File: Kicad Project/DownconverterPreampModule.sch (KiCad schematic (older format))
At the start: 15 parts, among them U1 GALI-1+, U2 MCA1-85L+, U4 LMV751

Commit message: PCB Changes
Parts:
- added J6: Conn_01x02, Pin_Headers:Pin_Header_Straight_1x02_Pitch1.27mm, symbol Conn_01x02
- C2: footprint RadarComponents:100PAD -> RadarComponents:100PAD+GND2
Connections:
- net GND: now also J6.1 (Pin_1)
- net at R6.2, U4.1 (VOUT): now also J6.2 (Pin_2)
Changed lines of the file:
@@
 F 0 "C2" H 3225 3400 50  0000 L CNN
 F 1 "270pF" H 3225 3200 50  0000 L CNN
-F 2 "RadarComponents:100PAD" H 3238 3150 50  0001 C CNN
+F 2 "RadarComponents:100PAD+GND2" H 3238 3150 50  0001 C CNN
 F 3 "" H 3200 3300 50  0001 C CNN
 	1    3200 3300
@@
 $EndComp
 Wire Wire Line
-	7800 2200 7500 2200
-Wire Wire Line
-	7500 2200 7500 1000
-Wire Wire Line
-	7500 1000 8500 1000
-Text Notes 8600 1000 0    60   ~ 0
+	7500 2200 7800 2200
+Wire Wire Line
+	7500 900  7500 2200
+Text Notes 8900 850  0    60   ~ 0
 OUT
 $Comp
@@
 Wire Wire Line
 	7400 2800 7800 2800
+$Comp
+L Conn_01x02 J6
+U 1 1 5A0523B7
+P 8700 1000
+F 0 "J6" H 8700 1100 50  0000 C CNN
+F 1 "Conn_01x02" H 8700 800 50  0000 C CNN
+F 2 "Pin_Headers:Pin_Header_Straight_1x02_Pitch1.27mm" H 8700 1000 50  0001 C CNN
+F 3 "" H 8700 1000 50  0001 C CNN
+	1    8700 1000
+	1    0    0    1
+$EndComp
+$Comp
+L GND #PWR010
+U 1 1 5A05247F
+P 8500 1100
+F 0 "#PWR010" H 8500 850 50  0001 C CNN
+F 1 "GND" H 8500 950 50  0000 C CNN
+F 2 "" H 8500 1100 50  0001 C CNN
+F 3 "" H 8500 1100 50  0001 C CNN
+	1    8500 1100
+	1    0    0    -1
+$EndComp
+Wire Wire Line
+	7500 900  8500 900
+Wire Wire Line
+	8500 1000 8500 1100
 $EndSCHEMATC

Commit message: More PCB Updates
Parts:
- R2: footprint RadarComponents:100PAD -> RadarComponents:100PAD+GND
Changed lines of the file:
@@
 F 0 "R2" V 3330 2800 50  0000 C CNN
 F 1 "75" V 3250 2800 50  0000 C CNN
-F 2 "RadarComponents:100PAD" V 3180 2800 50  0001 C CNN
+F 2 "RadarComponents:100PAD+GND" V 3180 2800 50  0001 C CNN
 F 3 "" H 3250 2800 50  0001 C CNN
 	1    3250 2800

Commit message: PCB Edits post PDR
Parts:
- added R21: 51, Resistors_SMD:R_0603, symbol R
- C15, C4: value 270pF -> ?F
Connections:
- net +9V: no longer C16.1, U4.5 (V+)
- net GND: now also R21.1
- net at C15.2, U2.3 (IF): now also R21.2
- new net +3V3: C16.1, U4.5 (V+)
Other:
- moved on the sheet: C1, C15, C16, C2, C3, C4, J6, R1, R2, R3, R4, R5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

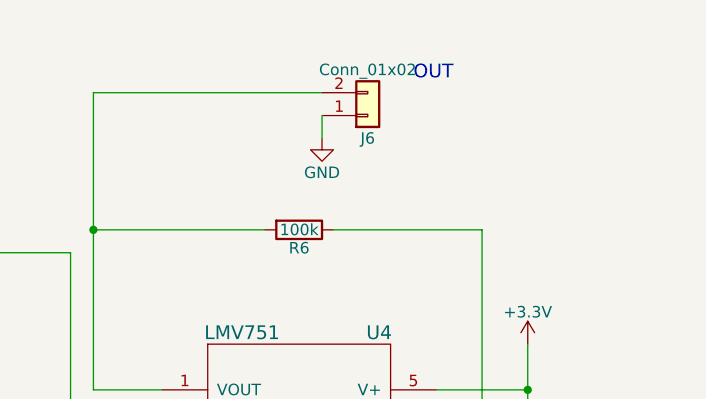
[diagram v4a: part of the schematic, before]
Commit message: Rev 2 update 1
Changes for Rev2:
Mounting Holes (duh)
Right Headers
HeadphoneJack
Added tantulum Caps at Regulators
Added UFL conns
Removed Resistive Divider
&
General layout stuff
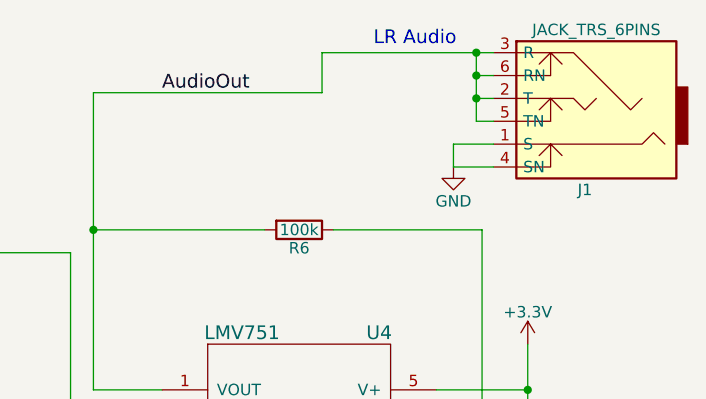
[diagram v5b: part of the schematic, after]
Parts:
- removed J6: Conn_01x02, Pin_Headers:Pin_Header_Straight_1x02_Pitch1.27mm, symbol Conn_01x02
- added J1: JACK_TRS_6PINS, RadarComponents:3.5mm_SMD, symbol JACK_TRS_6PINS
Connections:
- net GND: now also J1.1 (S), J1.4 (SN)
- net AudioOut: now reaches R6.2, U4.1 (VOUT)
- net AudioOut: now also J1.2 (T), J1.3 (R), J1.5 (TN), J1.6 (RN)
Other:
- note added: "LR Audio"
- note removed: "OUT"
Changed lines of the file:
@@
 Wire Wire Line
 	7950 975  7950 2275
-Text Notes 9350 925  0    60   ~ 0
-OUT
+Text Notes 9175 775  0    60   ~ 0
+LR Audio
 $Comp
 L R R6
@@
 	7850 2875 8250 2875
 $Comp
-L Conn_01x02 J6
-U 1 1 5A0523B7
-P 9150 1075
-F 0 "J6" H 9150 1175 50  0000 C CNN
-F 1 "Conn_01x02" H 9150 875 50  0000 C CNN
-F 2 "Pin_Headers:Pin_Header_Straight_1x02_Pitch1.27mm" H 9150 1075 50  0001 C CNN
-F 3 "" H 9150 1075 50  0001 C CNN
-	1    9150 1075
-	1    0    0    1
-$EndComp
-$Comp
 L GND #PWR09
 U 1 1 5A05247F
-P 8950 1175
-F 0 "#PWR09" H 8950 925 50  0001 C CNN
-F 1 "GND" H 8950 1025 50  0000 C CNN
-F 2 "" H 8950 1175 50  0001 C CNN
-F 3 "" H 8950 1175 50  0001 C CNN
-	1    8950 1175
+P 9525 1300
+F 0 "#PWR09" H 9525 1050 50  0001 C CNN
+F 1 "GND" H 9525 1150 50  0000 C CNN
+F 2 "" H 9525 1300 50  0001 C CNN
+F 3 "" H 9525 1300 50  0001 C CNN
+	1    9525 1300
 	1    0    0    -1
 $EndComp
 Wire Wire Line
 	7950 975  8950 975
-Wire Wire Line
-	8950 1075 8950 1175
 $Comp
 L +3.3V #PWR010
@@
 Wire Wire Line
 	6525 3275 6525 3675
+$Comp
+L JACK_TRS_6PINS J1
+U 1 1 5A1D11CD
+P 10100 1000
+F 0 "J1" H 10100 1400 50  0000 C CNN
+F 1 "JACK_TRS_6PINS" H 10050 700 50  0000 C CNN
+F 2 "RadarComponents:3.5mm_SMD" H 10200 850 50  0001 C CNN
+F 3 "" H 10200 850 50  0001 C CNN
+	1    10100 1000
+	-1   0    0    1
+$EndComp
+Wire Wire Line
+	8950 975  8950 800
+Wire Wire Line
+	8950 800  9700 800
+Wire Wire Line
+	9700 900  9625 900
+Wire Wire Line
+	9625 800  9625 1100
+Connection ~ 9625 800
+Wire Wire Line
+	9625 1000 9700 1000
+Connection ~ 9625 900
+Wire Wire Line
+	9625 1100 9700 1100
+Connection ~ 9625 1000
+Wire Wire Line
+	9700 1200 9525 1200
+Wire Wire Line
+	9525 1200 9525 1300
+Wire Wire Line
+	9525 1300 9700 1300
+Text Label 8250 975  0    60   ~ 0
+AudioOut
 $EndSCHEMATC

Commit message: More Routing
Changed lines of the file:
@@
 Wire Wire Line
 	9525 1300 9700 1300
-Text Label 8250 975  0    60   ~ 0
+Text GLabel 7950 1000 0    60   Input ~ 0
 AudioOut
 $EndSCHEMATC

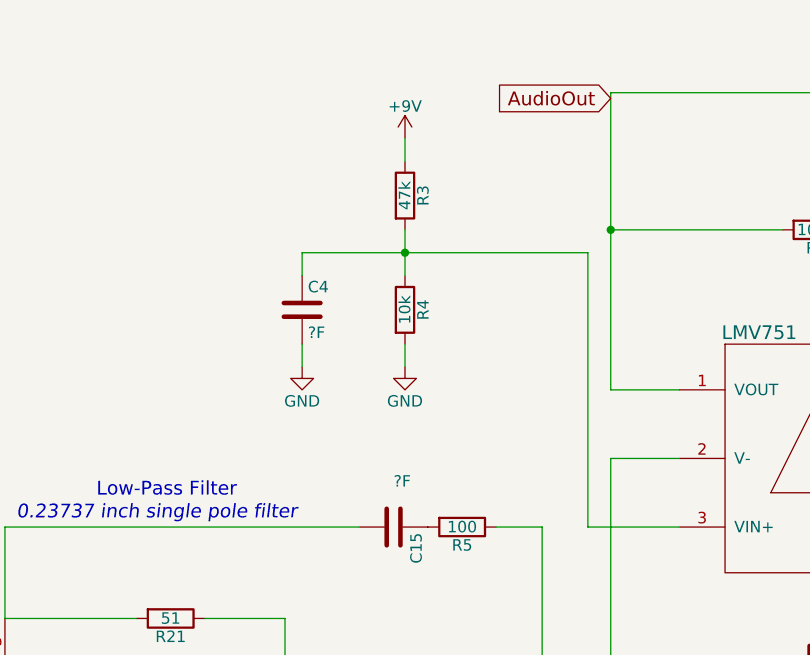
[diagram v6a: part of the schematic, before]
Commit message: Damian's almost to rev 2 completion, needs audio amps
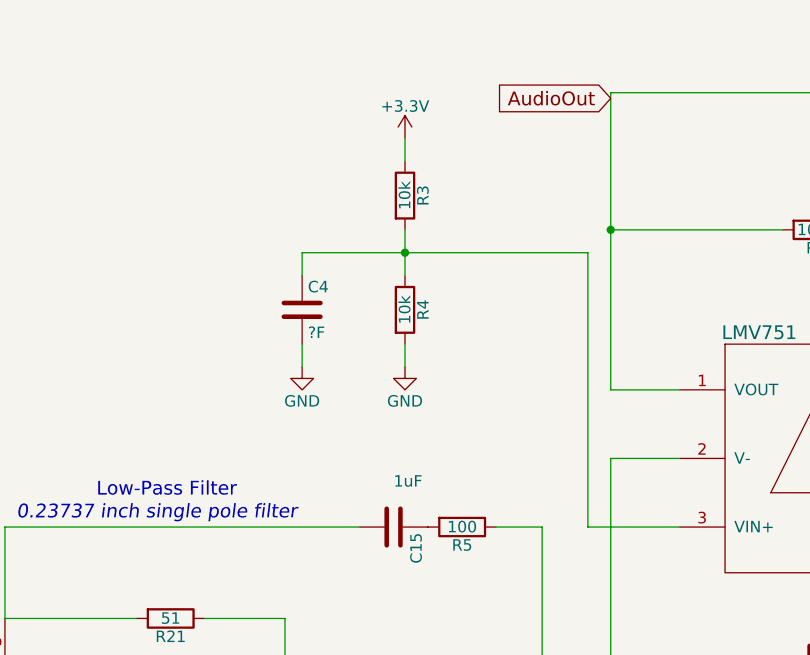
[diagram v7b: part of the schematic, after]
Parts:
- C15: value ?F -> 1uF
- C2: footprint RadarComponents:100PAD+GND2 -> RadarComponents:100PAD+GND3
- R3: value 47k -> 10k
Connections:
- net +3V3: now also R3.1
- net +9V: no longer R3.1
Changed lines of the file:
@@
 F 0 "C2" H 3675 3475 50  0000 L CNN
 F 1 "270pF" H 3675 3275 50  0000 L CNN
-F 2 "RadarComponents:100PAD+GND2" H 3688 3225 50  0001 C CNN
+F 2 "RadarComponents:100PAD+GND3" H 3688 3225 50  0001 C CNN
 F 3 "" H 3650 3375 50  0001 C CNN
 	1    3650 3375
@@
 P 7000 2875
 F 0 "C15" H 7025 2975 50  0000 L CNN
-F 1 "?F" V 6800 2875 50  0000 L CNN
+F 1 "1uF" V 6800 2875 50  0000 L CNN
 F 2 "Capacitors_SMD:C_0603" H 7038 2725 50  0001 C CNN
 F 3 "" H 7000 2875 50  0001 C CNN
@@
 P 7050 1425
 F 0 "R3" V 7130 1425 50  0000 C CNN
-F 1 "47k" V 7050 1425 50  0000 C CNN
+F 1 "10k" V 7050 1425 50  0000 C CNN
 F 2 "Resistors_SMD:R_0603" V 6980 1425 50  0001 C CNN
 F 3 "" H 7050 1425 50  0001 C CNN
@@
 	1    0    0    -1
 $EndComp
-$Comp
-L +9V #PWR08
-U 1 1 5A039E5F
-P 7050 1175
-F 0 "#PWR08" H 7050 1025 50  0001 C CNN
-F 1 "+9V" H 7050 1315 50  0000 C CNN
-F 2 "" H 7050 1175 50  0001 C CNN
-F 3 "" H 7050 1175 50  0001 C CNN
-	1    7050 1175
-	1    0    0    -1
-$EndComp
 Wire Wire Line
 	6600 2075 6600 2175
@@
 	7850 2875 8250 2875
 $Comp
-L GND #PWR09
+L GND #PWR08
 U 1 1 5A05247F
 P 9525 1300
-F 0 "#PWR09" H 9525 1050 50  0001 C CNN
+F 0 "#PWR08" H 9525 1050 50  0001 C CNN
 F 1 "GND" H 9525 1150 50  0000 C CNN
 F 2 "" H 9525 1300 50  0001 C CNN
@@
 	7950 975  8950 975
 $Comp
-L +3.3V #PWR010
+L +3.3V #PWR09
 U 1 1 5A06409C
 P 9850 2075
-F 0 "#PWR010" H 9850 1925 50  0001 C CNN
+F 0 "#PWR09" H 9850 1925 50  0001 C CNN
 F 1 "+3.3V" H 9850 2215 50  0000 C CNN
 F 2 "" H 9850 2075 50  0001 C CNN
@@
 $EndComp
 $Comp
-L GND #PWR011
+L GND #PWR010
 U 1 1 5A064555
 P 6525 3675
-F 0 "#PWR011" H 6525 3425 50  0001 C CNN
+F 0 "#PWR010" H 6525 3425 50  0001 C CNN
 F 1 "GND" H 6525 3525 50  0000 C CNN
 F 2 "" H 6525 3675 50  0001 C CNN
@@
 Text GLabel 7950 1000 0    60   Input ~ 0
 AudioOut
+$Comp
+L +3.3V #PWR011
+U 1 1 5A1DBC63
+P 7050 1175
+F 0 "#PWR011" H 7050 1025 50  0001 C CNN
+F 1 "+3.3V" H 7050 1315 50  0000 C CNN
+F 2 "" H 7050 1175 50  0001 C CNN
+F 3 "" H 7050 1175 50  0001 C CNN
+	1    7050 1175
+	1    0    0    -1
+$EndComp
 $EndSCHEMATC

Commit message: Rev 2?
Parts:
- added C27, C31: .68nF, Capacitors_SMD:C_0603, symbol C
- added C28, C30: 1uF, Capacitors_SMD:C_0603, symbol C
- added C29, C32: 270pF, Capacitors_SMD:C_0603, symbol C
- added J3: CONN_01X04, symbol CONN_01X04
- added R25: 1K, Resistors_SMD:R_0603, symbol R
- added R26: 10K, Resistors_SMD:R_0603, symbol R
- added R27: 100k, Resistors_SMD:R_0603, symbol R
- added U21: TPL0501, symbol TPL0501
- added U22, U23: LMV751, RadarComponents:SOT23-5, symbol LMV751
- R5: value 100 -> 1K
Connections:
- net +3V3: now also C16.2, C29.2, C32.2, U21.2 (VDD), U22.5 (V+), U23.5 (V+); no longer C16.1
- net AudioOut: now also C31.1, R27.1, U23.1 (VOUT); no longer R6.2, U4.1 (VOUT)
- net GND: now also C16.1, C29.1, C32.1, J3.4 (P4), U21.3 (GND), U22.2 (V-), U23.2 (V-); no longer C16.2
- net RawIF: now reaches C15.2, R21.2, U2.3 (IF)
- net VCC/2: now reaches C4.1, R3.2, R4.1, U4.3 (VIN+)
- net VCC/2: now also U22.3 (VIN+), U23.3 (VIN+)
- net at R5.1, U4.4 (VIN-): now also R6.2, C27.2; no longer R6.1
- new net: C27.1, C28.2, R6.1, U4.1 (VOUT)
- new net: C30.2, U21.8 (H), U22.1 (VOUT)
- new net: R25.1, U21.1 (W), U22.4 (VIN-)
- new net: C31.2, R26.1, R27.2, U23.4 (VIN-)
- new net: C28.1, R25.2
- new net: C30.1, R26.2
- new net DIN: J3.2 (P2), U21.5 (DIN)
- new net SCLK: J3.1 (P1), U21.4 (SCLK)
- new net ~CS: J3.3 (P3), U21.6 (~CS)
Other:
- moved on the sheet: C1, C15, C16, C2, C3, C4, J1, R1, R2, R21, R3, R4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
